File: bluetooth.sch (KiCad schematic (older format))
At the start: 45 parts, among them P16 CONN_2, P17 CONN_1, P18 CONN_1, P19 CONN_1, P20 CONN_1, P21 CONN_1, P22 CONN_1, P23 CONN_1, P24 CONN_1, P25 CONN_1, P28 CONN_1, P29 CONN_1, Q1 MOSFET_N, SW2 SPST, U2 TAR5SB33, U3 HT7750A, U4 LTC4054, U5 WT12_BLUEGIGA

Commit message: Finish Rev. A
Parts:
- added R17, R18: R, symbol R
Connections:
- net labels added: BT_LIPO
- wire segments 107 -> 110
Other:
- note added: "Voltage Divider for ADC\nZ<=10KOhm"
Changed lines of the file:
@@
 encoding utf-8
 Sheet 2 2
-Title ""
-Date ""
-Rev ""
-Comp ""
+Title "HHKB Alt Controller"
+Date "2013/06/17"
+Rev "A"
+Comp "TMK kbd"
 Comment1 ""
 Comment2 ""
@@
 $EndDescr
 $Comp
-L GND #PWR030
+L GND #PWR031
 U 1 1 51AFD3B1
 P 9450 3500
-F 0 "#PWR030" H 9450 3500 30  0001 C CNN
+F 0 "#PWR031" H 9450 3500 30  0001 C CNN
 F 1 "GND" H 9450 3430 30  0001 C CNN
 F 2 "" H 9450 3500 60  0000 C CNN
@@
 $EndComp
 $Comp
-L GND #PWR031
+L GND #PWR032
 U 1 1 51AFD3CA
 P 7200 3500
-F 0 "#PWR031" H 7200 3500 30  0001 C CNN
+F 0 "#PWR032" H 7200 3500 30  0001 C CNN
 F 1 "GND" H 7200 3430 30  0001 C CNN
 F 2 "" H 7200 3500 60  0000 C CNN
@@
 	-1   0    0    1
 $EndComp
-Text Notes 6200 6450 0    60   ~ 0
+Text Notes 5700 6200 0    60   ~ 0
 Lipo Battery\nJST connector
 $Comp
-L GND #PWR032
+L GND #PWR033
 U 1 1 51AFD4B7
 P 7050 6500
-F 0 "#PWR032" H 7050 6500 30  0001 C CNN
+F 0 "#PWR033" H 7050 6500 30  0001 C CNN
 F 1 "GND" H 7050 6430 30  0001 C CNN
 F 2 "" H 7050 6500 60  0000 C CNN
@@
 NoConn ~ 8350 1450
 $Comp
-L +3.3V #PWR033
+L +3.3V #PWR034
 U 1 1 51B15921
 P 5950 1200
-F 0 "#PWR033" H 5950 1160 30  0001 C CNN
+F 0 "#PWR034" H 5950 1160 30  0001 C CNN
 F 1 "+3.3V" H 5950 1310 30  0000 C CNN
 F 2 "" H 5950 1200 60  0000 C CNN
@@
 VBAT
 $Comp
-L GND #PWR034
+L GND #PWR035
 U 1 1 51B36189
 P 1700 6900
-F 0 "#PWR034" H 1700 6900 30  0001 C CNN
+F 0 "#PWR035" H 1700 6900 30  0001 C CNN
 F 1 "GND" H 1700 6830 30  0001 C CNN
 F 2 "" H 1700 6900 60  0000 C CNN
@@
 $EndComp
 $Comp
-L GND #PWR035
+L GND #PWR036
 U 1 1 51B36198
 P 4450 6900
-F 0 "#PWR035" H 4450 6900 30  0001 C CNN
+F 0 "#PWR036" H 4450 6900 30  0001 C CNN
 F 1 "GND" H 4450 6830 30  0001 C CNN
 F 2 "" H 4450 6900 60  0000 C CNN
@@
 $EndComp
 $Comp
-L GND #PWR036
+L GND #PWR037
 U 1 1 51B36208
 P 3500 6900
-F 0 "#PWR036" H 3500 6900 30  0001 C CNN
+F 0 "#PWR037" H 3500 6900 30  0001 C CNN
 F 1 "GND" H 3500 6830 30  0001 C CNN
 F 2 "" H 3500 6900 60  0000 C CNN
@@
 $EndComp
 $Comp
-L GND #PWR037
+L GND #PWR038
 U 1 1 51B4212D
 P 1650 4950
-F 0 "#PWR037" H 1650 4950 30  0001 C CNN
+F 0 "#PWR038" H 1650 4950 30  0001 C CNN
 F 1 "GND" H 1650 4880 30  0001 C CNN
 F 2 "" H 1650 4950 60  0000 C CNN
@@
 $EndComp
 $Comp
-L GND #PWR038
+L GND #PWR039
 U 1 1 51B4213C
 P 3700 4950
-F 0 "#PWR038" H 3700 4950 30  0001 C CNN
+F 0 "#PWR039" H 3700 4950 30  0001 C CNN
 F 1 "GND" H 3700 4880 30  0001 C CNN
 F 2 "" H 3700 4950 60  0000 C CNN
@@
 $EndComp
 $Comp
-L GND #PWR039
+L GND #PWR040
 U 1 1 51B421C0
 P 2050 4950
-F 0 "#PWR039" H 2050 4950 30  0001 C CNN
+F 0 "#PWR040" H 2050 4950 30  0001 C CNN
 F 1 "GND" H 2050 4880 30  0001 C CNN
 F 2 "" H 2050 4950 60  0000 C CNN
@@
 $EndComp
 $Comp
-L GND #PWR040
+L GND #PWR041
 U 1 1 51B42259
 P 3400 5150
-F 0 "#PWR040" H 3400 5150 30  0001 C CNN
+F 0 "#PWR041" H 3400 5150 30  0001 C CNN
 F 1 "GND" H 3400 5080 30  0001 C CNN
 F 2 "" H 3400 5150 60  0000 C CNN
@@
 NOISE
 $Comp
-L +3.3V #PWR041
+L +3.3V #PWR042
 U 1 1 51B42324
 P 4100 4300
-F 0 "#PWR041" H 4100 4260 30  0001 C CNN
+F 0 "#PWR042" H 4100 4260 30  0001 C CNN
 F 1 "+3.3V" H 4100 4410 30  0000 C CNN
 F 2 "" H 4100 4300 60  0000 C CNN
@@
 $EndComp
 $Comp
-L GND #PWR042
+L GND #PWR043
 U 1 1 51B4294A
 P 1400 3750
-F 0 "#PWR042" H 1400 3750 30  0001 C CNN
+F 0 "#PWR043" H 1400 3750 30  0001 C CNN
 F 1 "GND" H 1400 3680 30  0001 C CNN
 F 2 "" H 1400 3750 60  0000 C CNN
@@
 $EndComp
 $Comp
-L +5V #PWR043
+L +5V #PWR044
 U 1 1 51B42AA7
 P 2100 1150
-F 0 "#PWR043" H 2100 1240 20  0001 C CNN
+F 0 "#PWR044" H 2100 1240 20  0001 C CNN
 F 1 "+5V" H 2100 1240 30  0000 C CNN
 F 2 "" H 2100 1150 60  0000 C CNN
@@
 $EndComp
 $Comp
-L +3.3V #PWR044
+L +3.3V #PWR045
 U 1 1 51B42AB6
 P 1200 1150
-F 0 "#PWR044" H 1200 1110 30  0001 C CNN
+F 0 "#PWR045" H 1200 1110 30  0001 C CNN
 F 1 "+3.3V" H 1200 1260 30  0000 C CNN
 F 2 "" H 1200 1150 60  0000 C CNN
@@
 $EndComp
 $Comp
-L GND #PWR045
+L GND #PWR046
 U 1 1 51B4304E
 P 10350 3700
-F 0 "#PWR045" H 10350 3700 30  0001 C CNN
+F 0 "#PWR046" H 10350 3700 30  0001 C CNN
 F 1 "GND" H 10350 3630 30  0001 C CNN
 F 2 "" H 10350 3700 60  0000 C CNN
@@
 $EndComp
 $Comp
-L GND #PWR046
+L GND #PWR047
 U 1 1 51B4305D
 P 6800 3150
-F 0 "#PWR046" H 6800 3150 30  0001 C CNN
+F 0 "#PWR047" H 6800 3150 30  0001 C CNN
 F 1 "GND" H 6800 3080 30  0001 C CNN
 F 2 "" H 6800 3150 60  0000 C CNN
@@
 $EndComp
 $Comp
-L GND #PWR047
+L GND #PWR048
 U 1 1 51B43F20
 P 9150 3850
-F 0 "#PWR047" H 9150 3850 30  0001 C CNN
+F 0 "#PWR048" H 9150 3850 30  0001 C CNN
 F 1 "GND" H 9150 3780 30  0001 C CNN
 F 2 "" H 9150 3850 60  0000 C CNN
@@
 $EndComp
 $Comp
-L GND #PWR048
+L GND #PWR049
 U 1 1 51B44001
 P 8500 6800
-F 0 "#PWR048" H 8500 6800 30  0001 C CNN
+F 0 "#PWR049" H 8500 6800 30  0001 C CNN
 F 1 "GND" H 8500 6730 30  0001 C CNN
 F 2 "" H 8500 6800 60  0000 C CNN
@@
 BT_DTR
 $Comp
-L GND #PWR049
+L GND #PWR050
 U 1 1 51B8A40C
 P 3450 3750
-F 0 "#PWR049" H 3450 3750 30  0001 C CNN
+F 0 "#PWR050" H 3450 3750 30  0001 C CNN
 F 1 "GND" H 3450 3680 30  0001 C CNN
 F 2 "" H 3450 3750 60  0000 C CNN
@@
 $EndComp
 $Comp
-L +3.3V #PWR050
+L +3.3V #PWR051
 U 1 1 51B8A63B
 P 6650 4100
-F 0 "#PWR050" H 6650 4060 30  0001 C CNN
+F 0 "#PWR051" H 6650 4060 30  0001 C CNN
 F 1 "+3.3V" H 6650 4210 30  0000 C CNN
 F 2 "" H 6650 4100 60  0000 C CNN
@@
 $EndComp
 $Comp
-L GND #PWR051
+L GND #PWR052
 U 1 1 51B8A64A
 P 6700 4250
-F 0 "#PWR051" H 6700 4250 30  0001 C CNN
+F 0 "#PWR052" H 6700 4250 30  0001 C CNN
 F 1 "GND" H 6700 4180 30  0001 C CNN
 F 2 "" H 6700 4250 60  0000 C CNN
@@
 $EndComp
 $Comp
-L PWR_FLAG #FLG052
+L PWR_FLAG #FLG053
 U 1 1 51B8B9B3
 P 6800 1200
-F 0 "#FLG052" H 6800 1295 30  0001 C CNN
+F 0 "#FLG053" H 6800 1295 30  0001 C CNN
 F 1 "PWR_FLAG" H 6800 1380 30  0000 C CNN
 F 2 "" H 6800 1200 60  0000 C CNN
@@
 $EndComp
 $Comp
-L GND #PWR053
+L GND #PWR054
 U 1 1 51B8BF6B
 P 9050 6800
-F 0 "#PWR053" H 9050 6800 30  0001 C CNN
+F 0 "#PWR054" H 9050 6800 30  0001 C CNN
 F 1 "GND" H 9050 6730 30  0001 C CNN
 F 2 "" H 9050 6800 60  0000 C CNN
@@
 Wire Wire Line
 	6600 5700 6850 5700
-Wire Wire Line
-	6850 5700 6850 6050
-Connection ~ 6850 6050
 Connection ~ 7300 5550
 Wire Wire Line
@@
 $EndComp
 $Comp
-L GND #PWR054
+L GND #PWR055
 U 1 1 51BC0B97
 P 10200 5750
-F 0 "#PWR054" H 10200 5750 30  0001 C CNN
+F 0 "#PWR055" H 10200 5750 30  0001 C CNN
 F 1 "GND" H 10200 5680 30  0001 C CNN
 F 2 "" H 10200 5750 60  0000 C CNN
@@
 Text Notes 6800 5500 0    60   Italic 0
 SMT or TH
+$Comp
+L R R17
+U 1 1 51BE9662
+P 6850 6750
+F 0 "R17" V 6930 6750 50  0000 C CNN
+F 1 "R" V 6850 6750 50  0000 C CNN
+F 2 "" H 6850 6750 60  0000 C CNN
+F 3 "" H 6850 6750 60  0000 C CNN
+	1    6850 6750
+	1    0    0    -1
+$EndComp
+$Comp
+L R R18
+U 1 1 51BE9671
+P 6850 7350
+F 0 "R18" V 6930 7350 50  0000 C CNN
+F 1 "R" V 6850 7350 50  0000 C CNN
+F 2 "" H 6850 7350 60  0000 C CNN
+F 3 "" H 6850 7350 60  0000 C CNN
+	1    6850 7350
+	1    0    0    -1
+$EndComp
+$Comp
+L GND #PWR056
+U 1 1 51BE968F
+P 6850 7650
+F 0 "#PWR056" H 6850 7650 30  0001 C CNN
+F 1 "GND" H 6850 7580 30  0001 C CNN
+F 2 "" H 6850 7650 60  0000 C CNN
+F 3 "" H 6850 7650 60  0000 C CNN
+	1    6850 7650
+	1    0    0    -1
+$EndComp
+Wire Wire Line
+	6850 7000 6850 7100
+Wire Wire Line
+	6850 7600 6850 7650
+Wire Wire Line
+	6850 7050 6500 7050
+Connection ~ 6850 7050
+Text GLabel 6500 7050 0    60   Input ~ 0
+BT_LIPO
+Connection ~ 6850 6050
+Wire Wire Line
+	6850 5700 6850 6500
+Text Notes 5600 7550 0    60   ~ 0
+Voltage Divider for ADC\nZ<=10KOhm
 $EndSCHEMATC

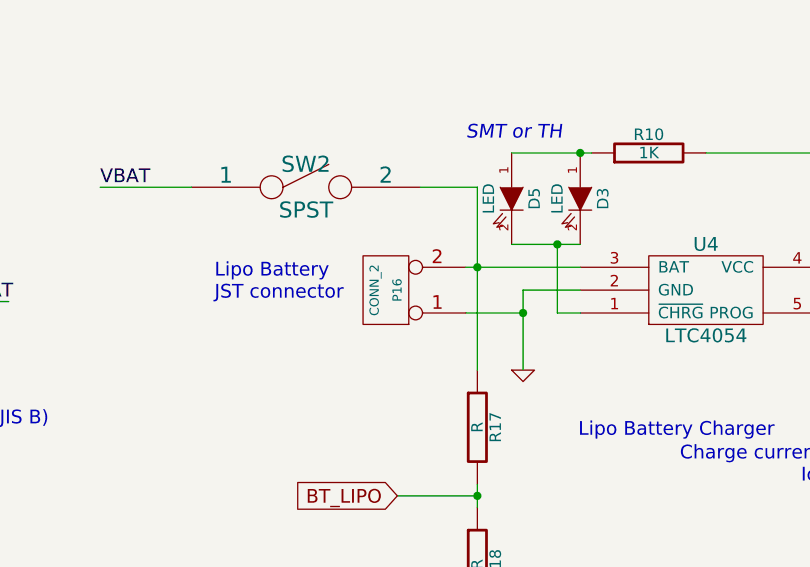
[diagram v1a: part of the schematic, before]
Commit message: Replace Lipo connector with SMT component
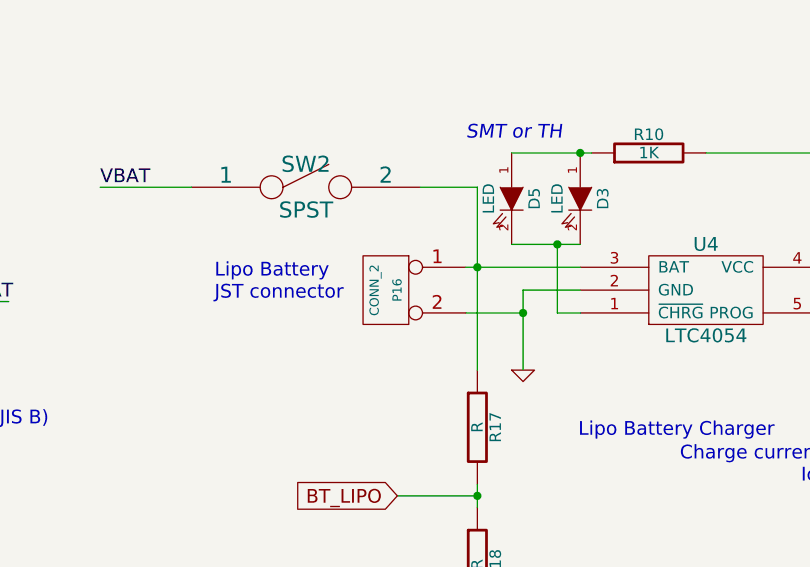
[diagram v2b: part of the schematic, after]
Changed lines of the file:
@@
 LIBS:contrib
 LIBS:valves
+LIBS:open-project
 LIBS:HHKB_controller-cache
 EELAYER 24 0
@@
 F 3 "" H 6450 6150 60  0000 C CNN
 	1    6450 6150
-	-1   0    0    1
+	-1   0    0    -1
 $EndComp
 Text Notes 5700 6200 0    60   ~ 0

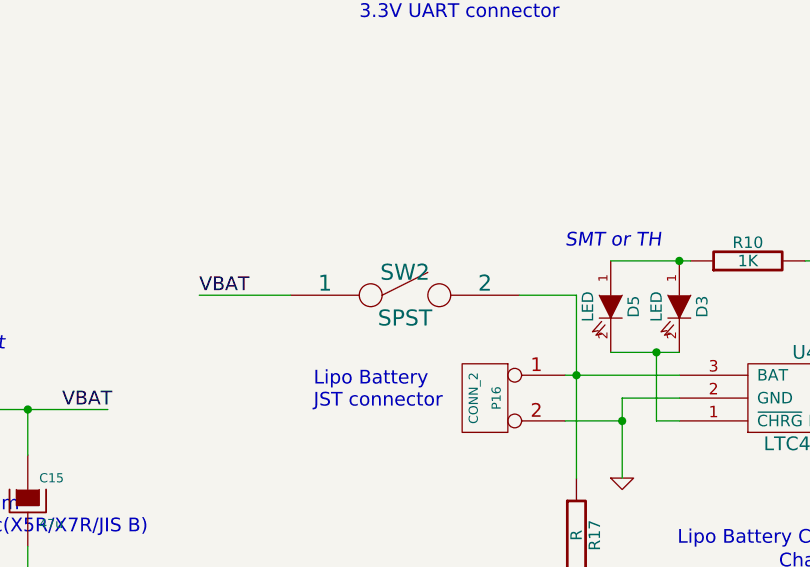
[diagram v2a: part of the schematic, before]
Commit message: Fix USB controller part
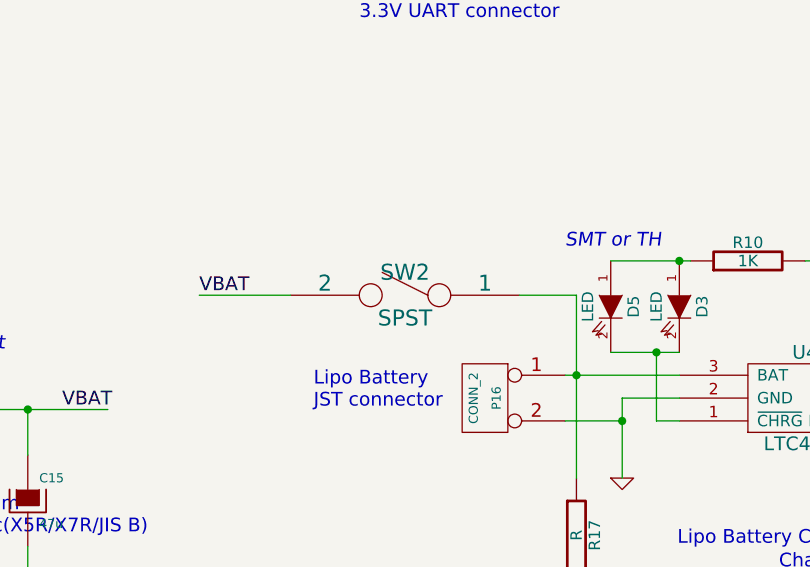
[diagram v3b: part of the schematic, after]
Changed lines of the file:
@@
 F 3 "" H 6100 5700 60  0000 C CNN
 	1    6100 5700
-	1    0    0    -1
+	-1   0    0    -1
 $EndComp
 Wire Wire Line

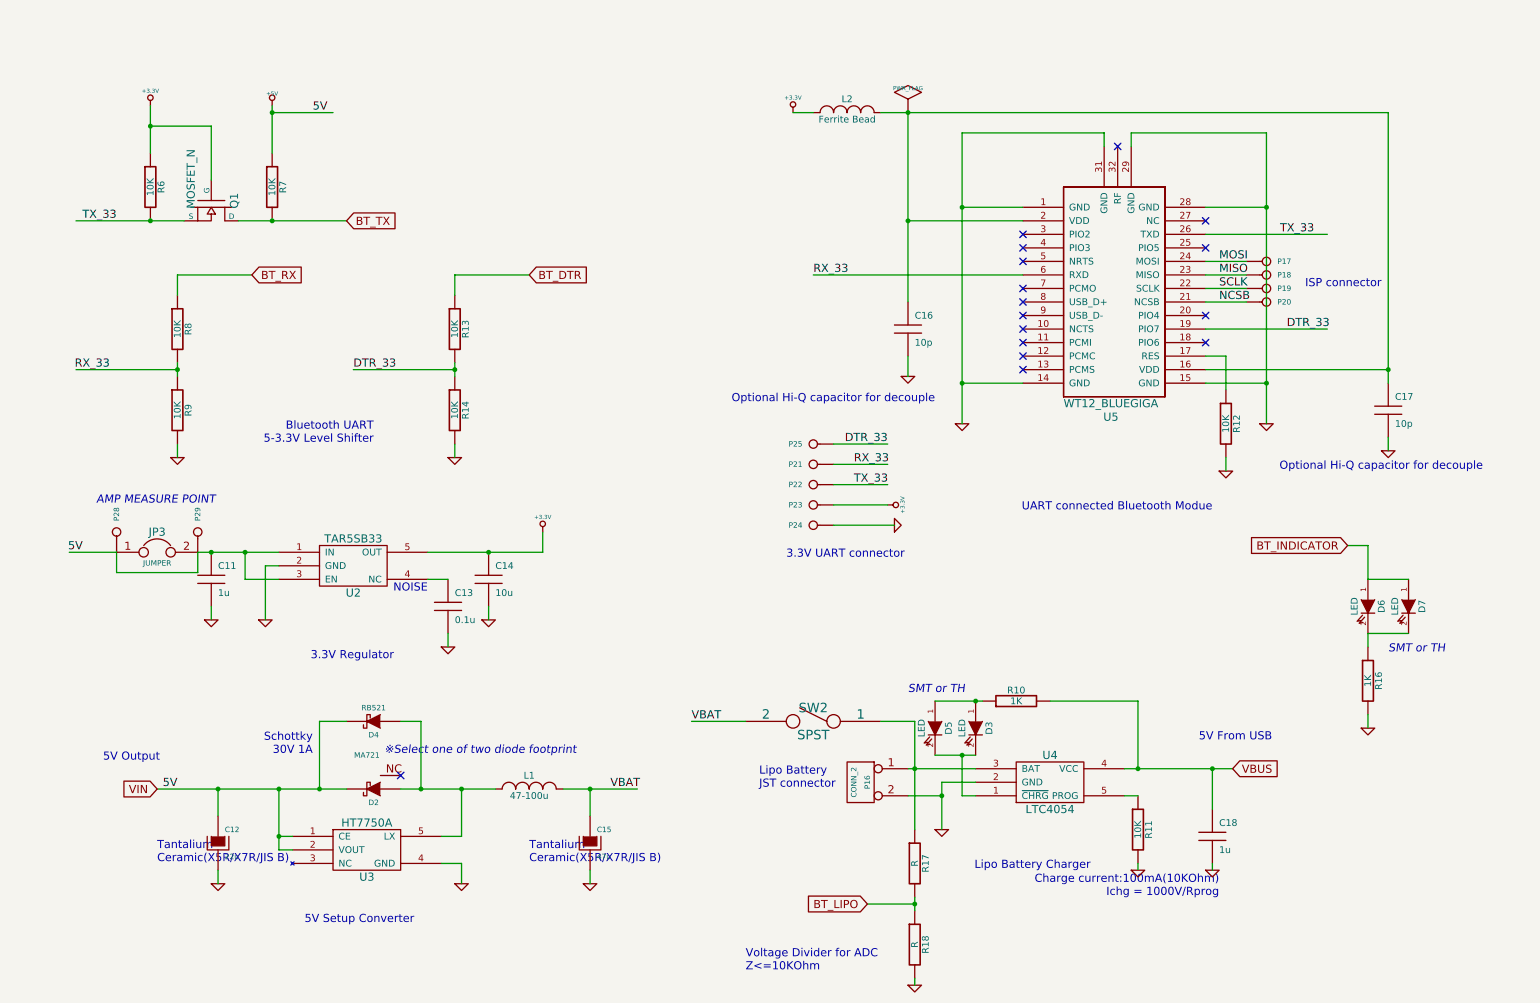
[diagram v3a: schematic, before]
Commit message: Add Power Source Selector
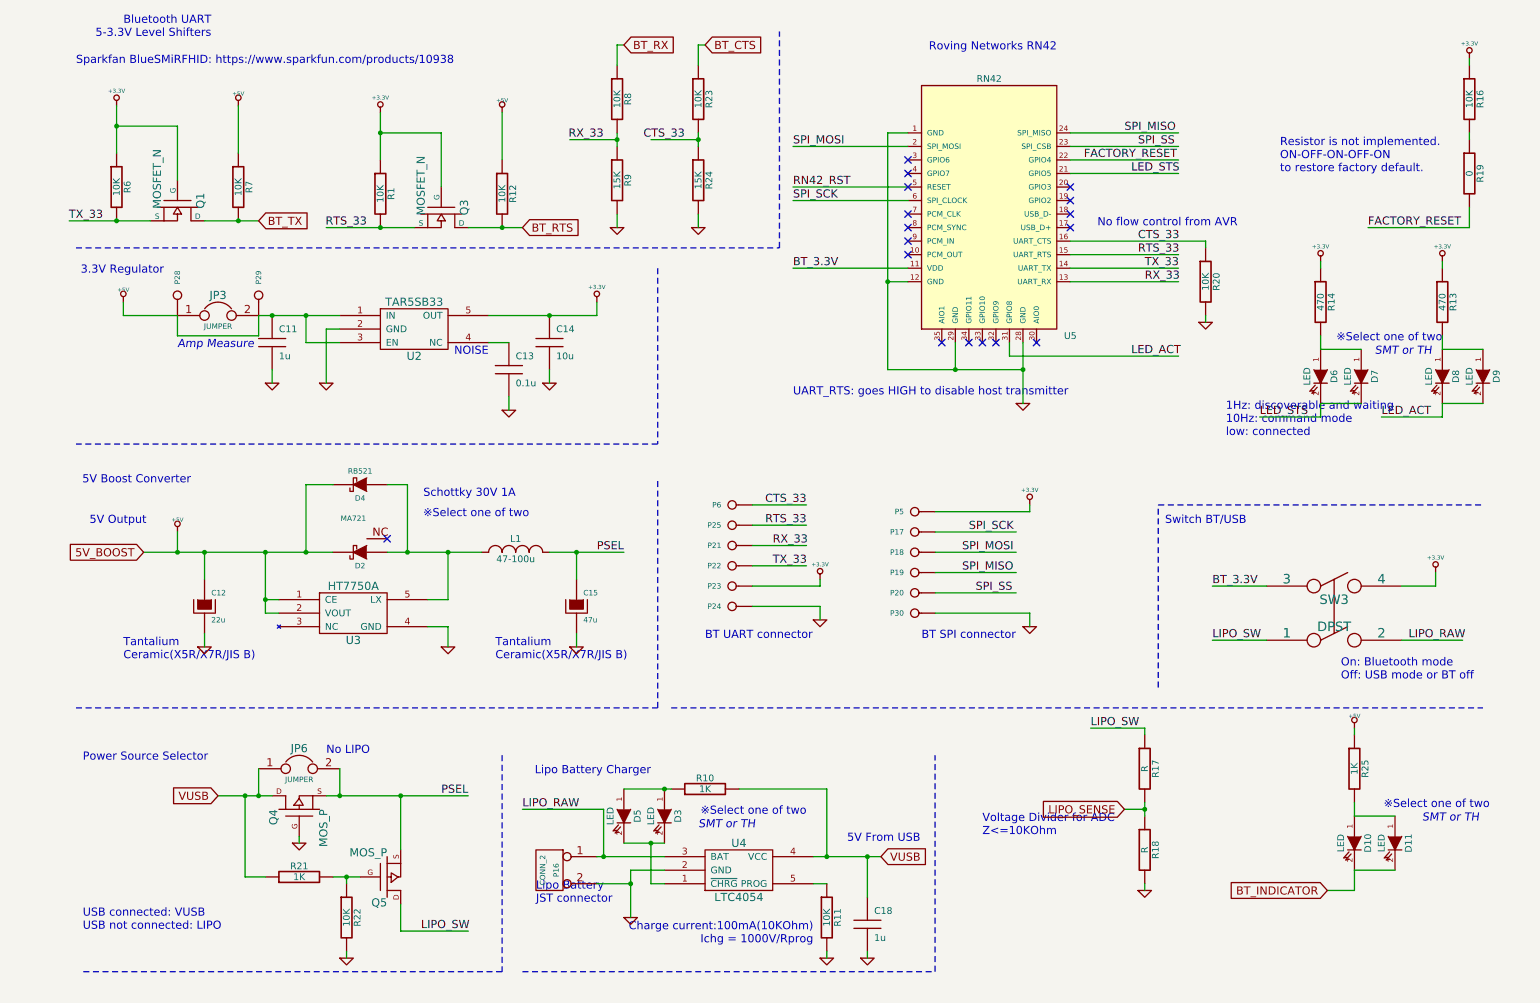
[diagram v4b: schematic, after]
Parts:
- removed C16, C17: 10p, symbol C
- removed L2: Ferrite Bead, symbol INDUCTOR_SMALL
- removed SW2: SPST, symbol SPST
- removed U5: WT12_BLUEGIGA, symbol WT12_BLUEGIGA
- added D10, D11, D8, D9: LED, symbol LED
- added JP6: JUMPER, symbol JUMPER
- added P30, P5, P6: CONN_1, symbol CONN_1
- added Q3: MOSFET_N, symbol MOSFET_N
- added Q4, Q5: MOS_P, symbol MOS_P
- added R1, R20, R22, R23: 10K, symbol R
- added R19: 0, symbol R
- added R21, R25: 1K, symbol R
- added R24: 15K, symbol R
- added SW3: DPST, symbol DPST
- added U5: RN42, symbol RN42
- R13, R14: value 10K -> 470
- R16: value 1K -> 10K
- R9: value 10K -> 15K
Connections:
- net labels added: 5V_BOOST, BT_3.3V, BT_CTS, BT_RTS, CTS_33, FACTORY_RESET, LED_ACT, LED_STS, LIPO_RAW, LIPO_SENSE, LIPO_SW, PSEL, RN42_RST, RTS_33, SPI_MISO, SPI_MOSI, SPI_SCK, SPI_SS, VUSB
- net labels removed: 5V, BT_DTR, BT_LIPO, DTR_33, MISO, MOSI, NCSB, SCLK, VBAT, VBUS, VIN
- wire segments 110 -> 157
- no-connect marks 16 -> 17
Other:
- note added: "1Hz: discoverable and waiting\n10Hz: command mode\nlow: connected"
- note added: "5V Boost Converter"
- note added: "Amp Measure"
- note added: "BT SPI connector"
- note added: "BT UART connector"
- note added: "Bluetooth UART\n5-3.3V Level Shifters"
- note added: "No LIPO"
- note added: "No flow control from AVR"
- note added: "On: Bluetooth mode\nOff: USB mode or BT off"
- note added: "Power Source Selector"
- note added: "Resistor is not implemented.\nON-OFF-ON-OFF-ON\nto restore factory default."
- note added: "Roving Networks RN42"
- note added: "Schottky 30V 1A"
- note added: "Sparkfan BlueSMiRFHID: https://www.sparkfun.com/products/10938"
- note added: "Switch BT/USB"
- note added: "UART_RTS: goes HIGH to disable host transmitter"
- note added: "USB connected: VUSB\nUSB not connected: LIPO"
- note added: "※Select one of two"
- note removed: "3.3V UART connector"
- note removed: "5V Setup Converter"
- note removed: "AMP MEASURE POINT"
- note removed: "Bluetooth UART\n5-3.3V Level Shifter"
- note removed: "ISP connector"
- note removed: "Optional Hi-Q capacitor for decouple"
- note removed: "Schottky\n30V 1A"
- note removed: "UART connected Bluetooth Modue"
- note removed: "※Select one of two diode footprint"
- moved on the sheet: C11, C12, C13, C14, C15, C18, D2, D3, D4, D5, D6, D7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
